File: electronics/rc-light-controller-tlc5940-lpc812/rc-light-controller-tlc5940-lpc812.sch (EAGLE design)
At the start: 40 parts, among them U2 TLC5940PWP

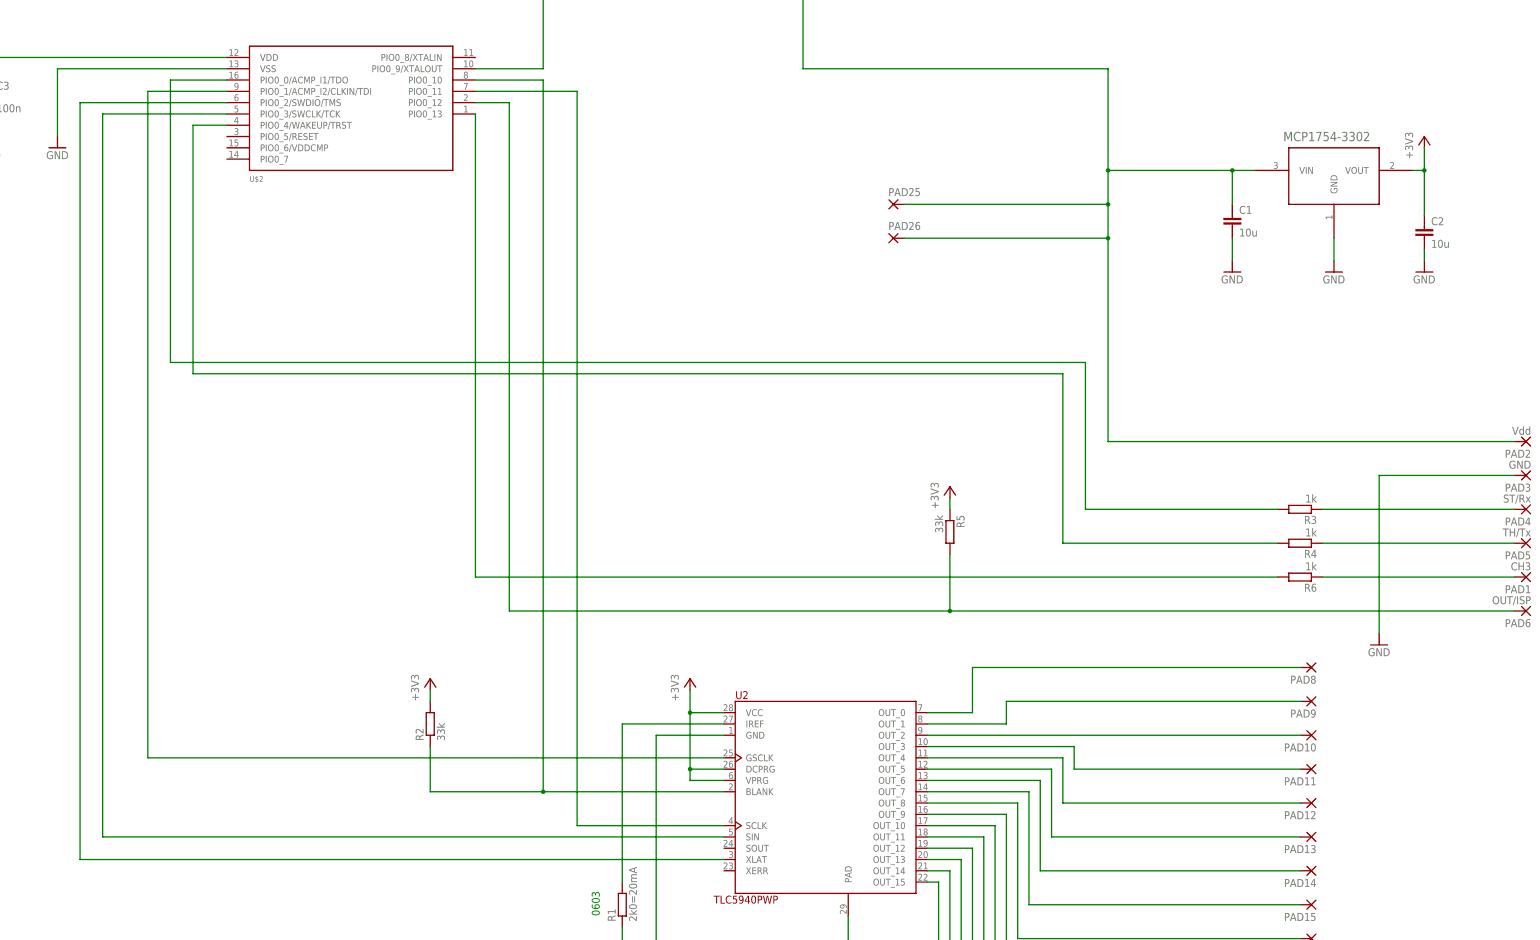
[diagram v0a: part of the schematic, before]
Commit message: Remove pull-ups and improve the board
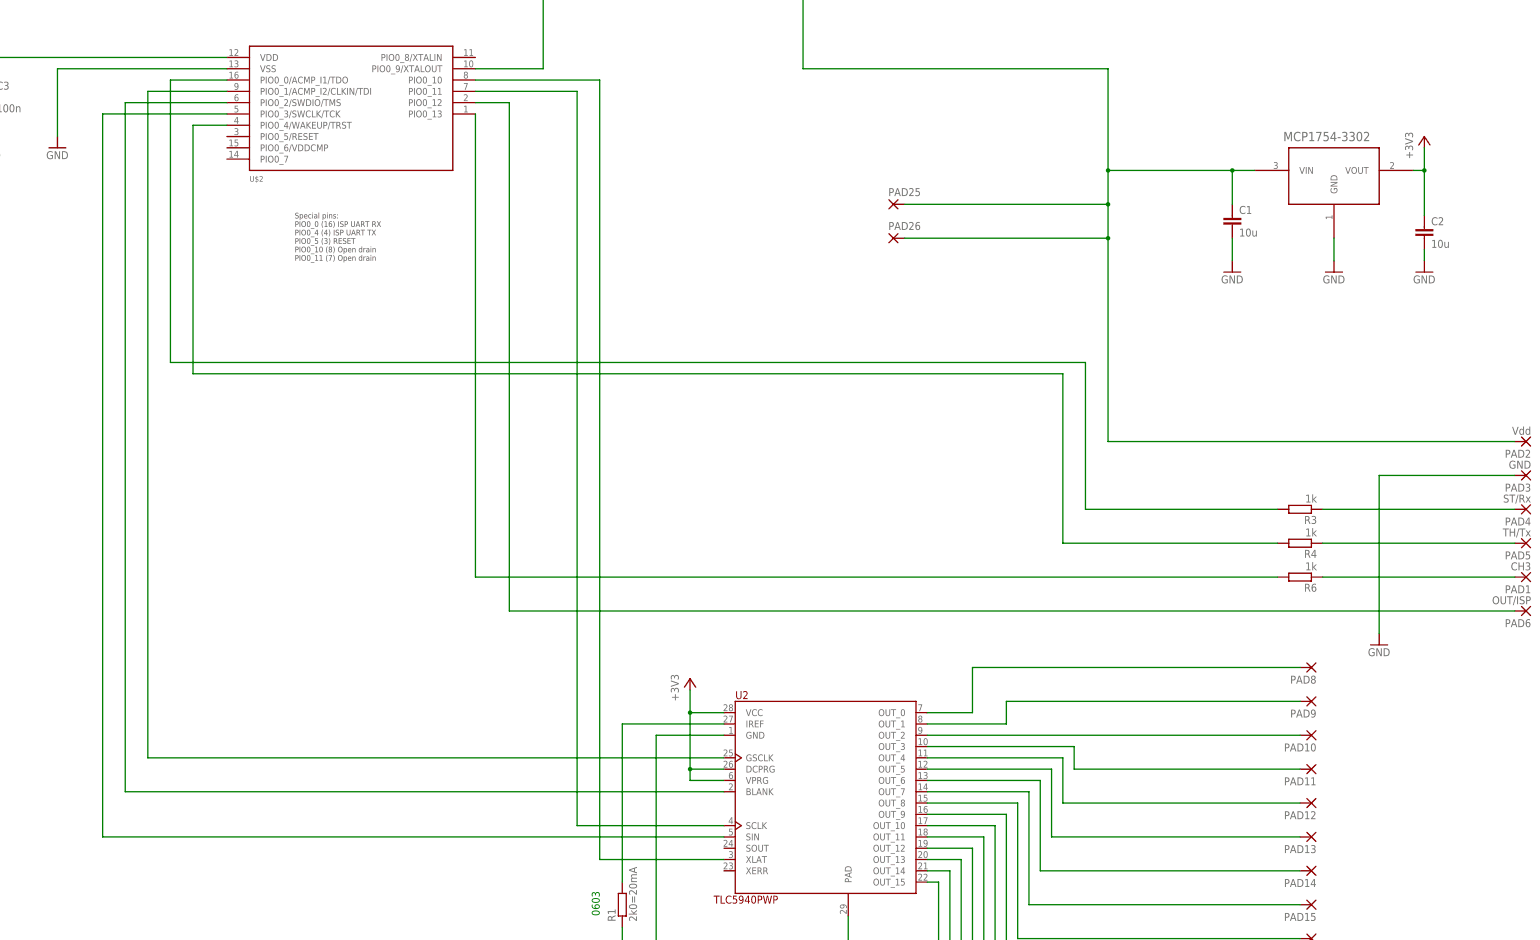
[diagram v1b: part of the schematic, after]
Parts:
- removed R2, R5: 33k, rcl:R-EU_R0603
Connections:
- net +3V3: no longer R2.2, R5.1
- net BLANK: now also U$2.PIO0_2/SWDIO/TMS; no longer R2.1, U$2.PIO0_10
- net N$20: no longer R5.2
- net SLAT: now also U$2.PIO0_10; no longer U$2.PIO0_2/SWDIO/TMS
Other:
- note added: "Special pins: PIO0_0 (16) ISP UART RX PIO0_4 (4) ISP UART TX PIO0_5 (3) RESET PIO0_10 (8) Open drain PIO0_11 (7) Open drain"
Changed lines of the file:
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@@
 <part name="GND8" library="supply1" deviceset="GND" device=""/>
 <part name="U$1" library="MCP1754" deviceset="MCP1754X-XXXXX/C" device=""/>
-<part name="R2" library="rcl" deviceset="R-EU_" device="R0603" value="33k"/>
-<part name="+3V4" library="supply1" deviceset="+3V3" device=""/>
 <part name="PAD2" library="wirepad" deviceset="SDM80X120" device="" value="Vdd"/>
 <part name="PAD3" library="wirepad" deviceset="SDM80X120" device="" value="GND"/>
@@
 <part name="R3" library="rcl" deviceset="R-EU_" device="R0603" value="1k"/>
 <part name="R4" library="rcl" deviceset="R-EU_" device="R0603" value="1k"/>
-<part name="R5" library="rcl" deviceset="R-EU_" device="R0603" value="33k"/>
 <part name="U$2" library="LPC810" deviceset="LPC812M101JDH16" device="" value="LPC812"/>
 <part name="PAD1" library="wirepad" deviceset="SDM80X120" device="" value="CH3"/>
 <part name="R6" library="rcl" deviceset="R-EU_" device="R0603" value="1k"/>
-<part name="+3V5" library="supply1" deviceset="+3V3" device=""/>
 <part name="D1" library="diode" deviceset="ES2D" device="" value="(Diode)"/>
 <part name="PAD7" library="wirepad" deviceset="SDM80X120" device="" value="GND"/>
@@
 <plain>
 <text x="-50.8" y="7.62" size="1.778" layer="91" rot="R90">0603</text>
+<text x="-119.38" y="154.94" size="1.27" layer="97">Special pins:
+PIO0_0 (16) ISP UART RX
+PIO0_4 (4) ISP UART TX
+PIO0_5 (3) RESET
+PIO0_10 (8) Open drain
+PIO0_11 (7) Open drain</text>
 </plain>
 <instances>
@@
 <instance part="GND8" gate="1" x="-187.96" y="180.34"/>
 <instance part="U$1" gate="A" x="114.3" y="175.26"/>
-<instance part="R2" gate="G$1" x="-88.9" y="50.8" rot="R90"/>
-<instance part="+3V4" gate="G$1" x="-88.9" y="60.96"/>
 <instance part="PAD2" gate="G$1" x="157.48" y="114.3" rot="R180"/>
 <instance part="PAD3" gate="G$1" x="157.48" y="106.68" rot="R180"/>
@@
 <instance part="R3" gate="G$1" x="106.68" y="99.06" rot="R180"/>
 <instance part="R4" gate="G$1" x="106.68" y="91.44" rot="R180"/>
-<instance part="R5" gate="G$1" x="27.94" y="93.98" rot="R270"/>
 <instance part="U$2" gate="G$1" x="-106.68" y="190.5"/>
 <instance part="PAD1" gate="G$1" x="157.48" y="83.82" rot="R180"/>
 <instance part="R6" gate="G$1" x="106.68" y="83.82" rot="R180"/>
-<instance part="+3V5" gate="G$1" x="27.94" y="104.14"/>
 <instance part="D1" gate="G$1" x="12.7" y="236.22"/>
 <instance part="PAD7" gate="G$1" x="35.56" y="228.6" rot="R180"/>
@@
 <pinref part="C2" gate="G$1" pin="1"/>
 </segment>
-<segment>
-<wire x1="-88.9" y1="55.88" x2="-88.9" y2="58.42" width="0.1524" layer="91"/>
-<pinref part="R2" gate="G$1" pin="2"/>
-<pinref part="+3V4" gate="G$1" pin="+3V3"/>
-</segment>
-<segment>
-<pinref part="R5" gate="G$1" pin="1"/>
-<pinref part="+3V5" gate="G$1" pin="+3V3"/>
-<wire x1="27.94" y1="99.06" x2="27.94" y2="101.6" width="0.1524" layer="91"/>
-</segment>
 </net>
 <net name="GND" class="0">
@@
 <net name="SLAT" class="0">
 <segment>
-<wire x1="-134.62" y1="190.5" x2="-167.64" y2="190.5" width="0.1524" layer="91"/>
-<wire x1="-167.64" y1="190.5" x2="-167.64" y2="20.32" width="0.1524" layer="91"/>
-<wire x1="-167.64" y1="20.32" x2="-22.86" y2="20.32" width="0.1524" layer="91"/>
+<wire x1="-50.8" y1="195.58" x2="-50.8" y2="20.32" width="0.1524" layer="91"/>
+<wire x1="-50.8" y1="20.32" x2="-22.86" y2="20.32" width="0.1524" layer="91"/>
 <pinref part="U2" gate="G$1" pin="XLAT"/>
+<pinref part="U$2" gate="G$1" pin="PIO0_10"/>
+<wire x1="-78.74" y1="195.58" x2="-50.8" y2="195.58" width="0.1524" layer="91"/>
+</segment>
+</net>
+<net name="BLANK" class="0">
+<segment>
+<wire x1="-22.86" y1="35.56" x2="-157.48" y2="35.56" width="0.1524" layer="91"/>
+<wire x1="-157.48" y1="35.56" x2="-157.48" y2="190.5" width="0.1524" layer="91"/>
+<pinref part="U2" gate="G$1" pin="BLANK"/>
 <pinref part="U$2" gate="G$1" pin="PIO0_2/SWDIO/TMS"/>
-</segment>
-</net>
-<net name="BLANK" class="0">
-<segment>
-<wire x1="-22.86" y1="35.56" x2="-63.5" y2="35.56" width="0.1524" layer="91"/>
-<wire x1="-63.5" y1="35.56" x2="-63.5" y2="195.58" width="0.1524" layer="91"/>
-<wire x1="-63.5" y1="195.58" x2="-78.74" y2="195.58" width="0.1524" layer="91"/>
-<wire x1="-88.9" y1="45.72" x2="-88.9" y2="35.56" width="0.1524" layer="91"/>
-<wire x1="-88.9" y1="35.56" x2="-63.5" y2="35.56" width="0.1524" layer="91"/>
-<junction x="-63.5" y="35.56"/>
-<pinref part="U2" gate="G$1" pin="BLANK"/>
-<pinref part="R2" gate="G$1" pin="1"/>
-<pinref part="U$2" gate="G$1" pin="PIO0_10"/>
+<wire x1="-134.62" y1="190.5" x2="-157.48" y2="190.5" width="0.1524" layer="91"/>
 </segment>
 </net>
@@
 <net name="N$20" class="0">
 <segment>
-<pinref part="R5" gate="G$1" pin="2"/>
-<wire x1="27.94" y1="88.9" x2="27.94" y2="76.2" width="0.1524" layer="91"/>
-<wire x1="27.94" y1="76.2" x2="154.94" y2="76.2" width="0.1524" layer="91"/>
-<wire x1="27.94" y1="76.2" x2="-71.12" y2="76.2" width="0.1524" layer="91"/>
+<wire x1="-71.12" y1="76.2" x2="154.94" y2="76.2" width="0.1524" layer="91"/>
 <wire x1="-71.12" y1="76.2" x2="-71.12" y2="190.5" width="0.1524" layer="91"/>
 <wire x1="-71.12" y1="190.5" x2="-78.74" y2="190.5" width="0.1524" layer="91"/>
 <pinref part="U$2" gate="G$1" pin="PIO0_12"/>
 <pinref part="PAD6" gate="G$1" pin="P"/>
-<junction x="27.94" y="76.2"/>
 </segment>
 </net>
@@
 </schematic>
 </drawing>
+<compatibility>
+<note version="6.3" minversion="6.2.2" severity="warning">
+Since Version 6.2.2 text objects can contain more than one line,
+which will not be processed correctly with this version.
+</note>
+</compatibility>
 </eagle>

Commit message: Improve schematic and tweak the board
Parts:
- removed PAD10, PAD11, PAD12, PAD13, PAD14, PAD15, PAD16, PAD17, PAD18, PAD19, PAD20, PAD21, PAD22, PAD23, PAD25, PAD26, PAD8, PAD9: (no value), wirepad:SMD50X100
- removed PAD27: +5V, wirepad:SDM80X120
- removed PAD28: Data out, wirepad:SDM80X120
- removed PAD4: ST/Rx, wirepad:SDM80X120
- added PAD30: GND, wirepad:SDM80X120
- added PAD31: +5V, wirepad:SDM80X120
- added PAD32: Data out, wirepad:SDM80X120
- added PAD37, PAD50, PAD51, PAD52, PAD53, PAD54, PAD55, PAD56, PAD57, PAD58, PAD59, PAD60, PAD61, PAD62, PAD63, PAD64, PAD65, PAD66: (no value), wirepad:SMD50X100
- PAD1: value CH3 -> Vdd
- PAD2: value Vdd -> GND
- PAD3: value GND -> ST/Rx
- PAD6: value OUT/ISP -> CH3
- PAD7: value GND -> OUT/ISP
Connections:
- net N$2 renamed CH3
- net SLAT renamed XLAT
- net ST/CLK/RX renamed TH/TX
- net TH/DAT/TX renamed ST/RX
- removed net N$20: PAD6.P, U$2.PIO0_12
- removed net N$5: PAD28.P, U$2.PIO0_9/XTALOUT
- new net OUT/ISP: PAD7.P, U$2.PIO0_12
- new net WS2812-DATA-OUT: PAD32.P, U$2.PIO0_9/XTALOUT
- net GND: now also PAD2.P, PAD30.P; no longer PAD3.P, PAD7.P
- net N$1: now also PAD6.P; no longer PAD1.P
- net N$17: now also PAD3.P; no longer PAD4.P
- net N$3: now also PAD31.P; no longer PAD27.P
- net OUT0: now also PAD50.P; no longer PAD8.P
- net OUT1: now also PAD51.P; no longer PAD9.P
- net OUT10: now also PAD60.P; no longer PAD18.P
- net OUT11: now also PAD61.P; no longer PAD19.P
- net OUT12: now also PAD62.P; no longer PAD20.P
- net OUT13: now also PAD63.P; no longer PAD21.P
- net OUT14: now also PAD64.P; no longer PAD22.P
- net OUT15: now also PAD65.P; no longer PAD23.P
- net OUT2: now also PAD52.P; no longer PAD10.P
- net OUT3: now also PAD53.P; no longer PAD11.P
- net OUT4: now also PAD54.P; no longer PAD12.P
- net OUT5: now also PAD55.P; no longer PAD13.P
- net OUT6: now also PAD56.P; no longer PAD14.P
- net OUT7: now also PAD57.P; no longer PAD15.P
- net OUT8: now also PAD58.P; no longer PAD16.P
- net OUT9: now also PAD59.P; no longer PAD17.P
- net VIN: now also PAD1.P, PAD37.P, PAD66.P; no longer PAD2.P, PAD25.P, PAD26.P
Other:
- note added: "LED driver and outputs"
- note added: "Microcontroller"
- note added: "Servo in/out"
- note added: "Special pins: PIO0_0 (16) ISP UART RX PIO0_4 ( 4) ISP UART TX PIO0_5 ( 3) RESET PIO0_10 ( 8) Open drain PIO0_11 ( 7) Open drain"
- note added: "Voltage regulator"
- note added: "WS2812 LED output"
- note removed: "Special pins: PIO0_0 (16) ISP UART RX PIO0_4 (4) ISP UART TX PIO0_5 (3) RESET PIO0_10 (8) Open drain PIO0_11 (7) Open drain"
- moved on the sheet: C1, C2, C3, D1, PAD1, PAD2, PAD3, PAD5, PAD6, PAD7, R1, R3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

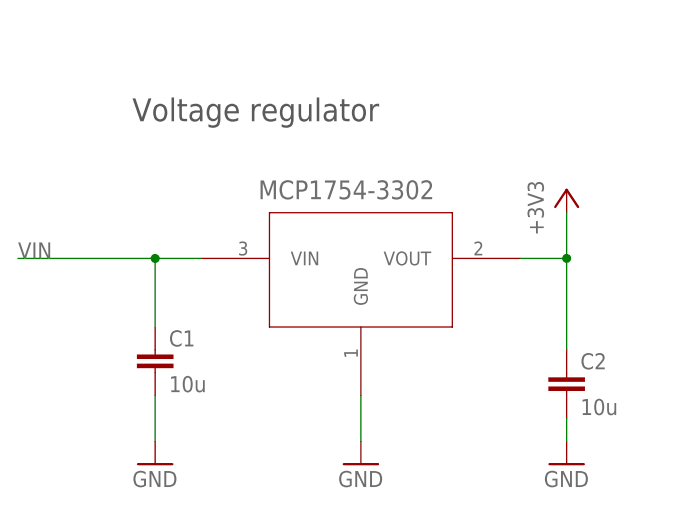
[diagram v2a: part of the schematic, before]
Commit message: Change to MCP1703 LDO
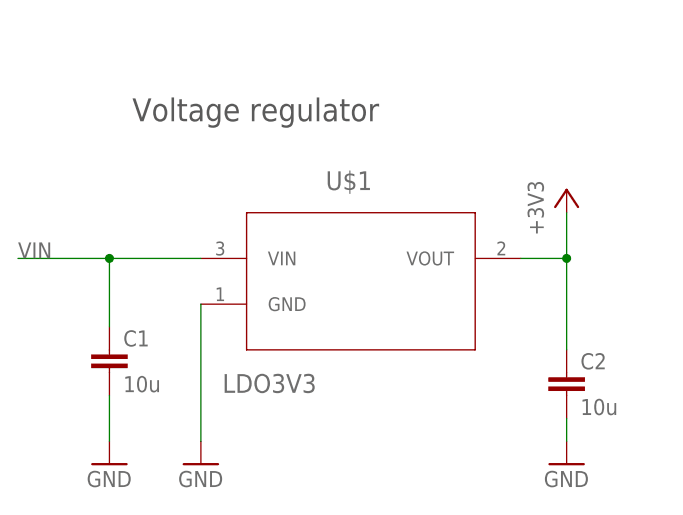
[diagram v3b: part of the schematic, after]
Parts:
- U$1: value MCP1754X-XXXXX/C -> LDO3V3; device MCP1754:MCP1754X-XXXXX/C -> MCP1703:MCP1703T-3302E/CB
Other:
- moved on the sheet: C1
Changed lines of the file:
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@@
 <part name="C3" library="rcl" deviceset="C-EU" device="C0805" value="100n"/>
 <part name="GND8" library="supply1" deviceset="GND" device=""/>
-<part name="U$1" library="MCP1754" deviceset="MCP1754X-XXXXX/C" device=""/>
+<part name="U$1" library="MCP1703" deviceset="MCP1703T-3302E/CB" device="" value="LDO3V3"/>
 <part name="PAD1" library="wirepad" deviceset="SDM80X120" device="" value="Vdd"/>
 <part name="PAD2" library="wirepad" deviceset="SDM80X120" device="" value="GND"/>
@@
 <instance part="C2" gate="G$1" x="91.44" y="43.18"/>
 <instance part="GND" gate="1" x="91.44" y="33.02"/>
-<instance part="GND5" gate="1" x="45.72" y="33.02"/>
-<instance part="GND6" gate="1" x="68.58" y="33.02"/>
+<instance part="GND5" gate="1" x="40.64" y="33.02"/>
+<instance part="GND6" gate="1" x="50.8" y="33.02"/>
 <instance part="+3V3" gate="G$1" x="91.44" y="63.5"/>
 <instance part="GND7" gate="1" x="53.34" y="165.1" rot="MR0"/>
 <instance part="C3" gate="G$1" x="119.38" y="119.38"/>
 <instance part="GND8" gate="1" x="119.38" y="106.68"/>
-<instance part="U$1" gate="A" x="68.58" y="55.88"/>
+<instance part="U$1" gate="A" x="68.58" y="55.88" smashed="yes">
+<attribute name="NAME" x="64.6684" y="63.4746" size="2.0828" layer="95" ratio="10" rot="SR0"/>
+<attribute name="VALUE" x="53.1876" y="40.9448" size="2.0828" layer="96" ratio="10" rot="SR0"/>
+</instance>
 <instance part="PAD1" gate="G$1" x="35.56" y="223.52" rot="MR180"/>
 <instance part="PAD2" gate="G$1" x="35.56" y="213.36" rot="MR180"/>
@@
 <instance part="PAD66" gate="1" x="370.84" y="119.38" rot="R180"/>
 <instance part="GND4" gate="1" x="266.7" y="175.26"/>
-<instance part="C1" gate="G$1" x="45.72" y="45.72"/>
+<instance part="C1" gate="G$1" x="40.64" y="45.72"/>
 <instance part="R3" gate="G$1" x="63.5" y="203.2" rot="MR180"/>
 <instance part="R4" gate="G$1" x="63.5" y="193.04" rot="MR180"/>
@@
 </segment>
 <segment>
-<wire x1="45.72" y1="35.56" x2="45.72" y2="40.64" width="0.1524" layer="91"/>
+<wire x1="40.64" y1="35.56" x2="40.64" y2="40.64" width="0.1524" layer="91"/>
 <pinref part="GND5" gate="1" pin="GND"/>
 <pinref part="C1" gate="G$1" pin="2"/>
@@
 </segment>
 <segment>
-<wire x1="68.58" y1="40.64" x2="68.58" y2="35.56" width="0.1524" layer="91"/>
+<wire x1="50.8" y1="50.8" x2="50.8" y2="35.56" width="0.1524" layer="91"/>
 <pinref part="U$1" gate="A" pin="GND"/>
 <pinref part="GND6" gate="1" pin="GND"/>
@@
 <net name="VIN" class="0">
 <segment>
-<wire x1="50.8" y1="55.88" x2="45.72" y2="55.88" width="0.1524" layer="91"/>
-<wire x1="45.72" y1="55.88" x2="30.48" y2="55.88" width="0.1524" layer="91"/>
-<wire x1="45.72" y1="48.26" x2="45.72" y2="55.88" width="0.1524" layer="91"/>
-<junction x="45.72" y="55.88"/>
+<wire x1="50.8" y1="55.88" x2="40.64" y2="55.88" width="0.1524" layer="91"/>
+<wire x1="40.64" y1="55.88" x2="30.48" y2="55.88" width="0.1524" layer="91"/>
+<wire x1="40.64" y1="48.26" x2="40.64" y2="55.88" width="0.1524" layer="91"/>
+<junction x="40.64" y="55.88"/>
 <pinref part="U$1" gate="A" pin="VIN"/>
 <pinref part="C1" gate="G$1" pin="1"/>
